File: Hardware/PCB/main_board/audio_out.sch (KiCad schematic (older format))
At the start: 28 parts, among them J12 Post_AB_amp, J13 Audio_out_jack, J6 AudioJack3, J9 Pre_AB_amp, Q1 BC857B, Q2 BC847B, Q3 BC847B, Q4 BC857B, U5 MCP6002-xSN

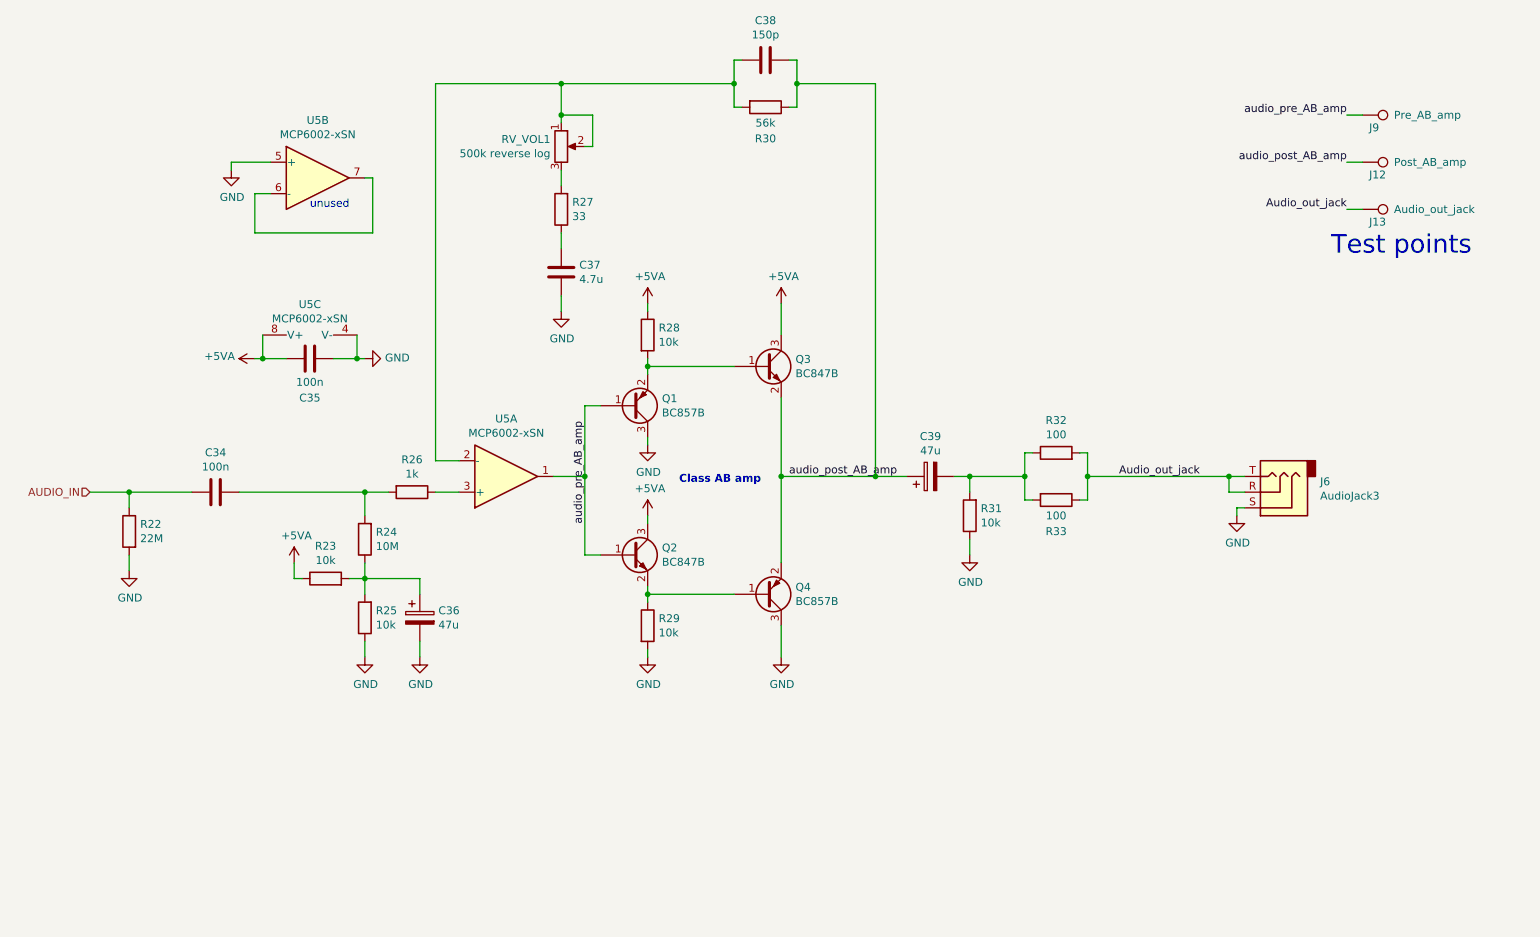
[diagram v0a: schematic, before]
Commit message: Use headphone amp IC instead of discrete amp
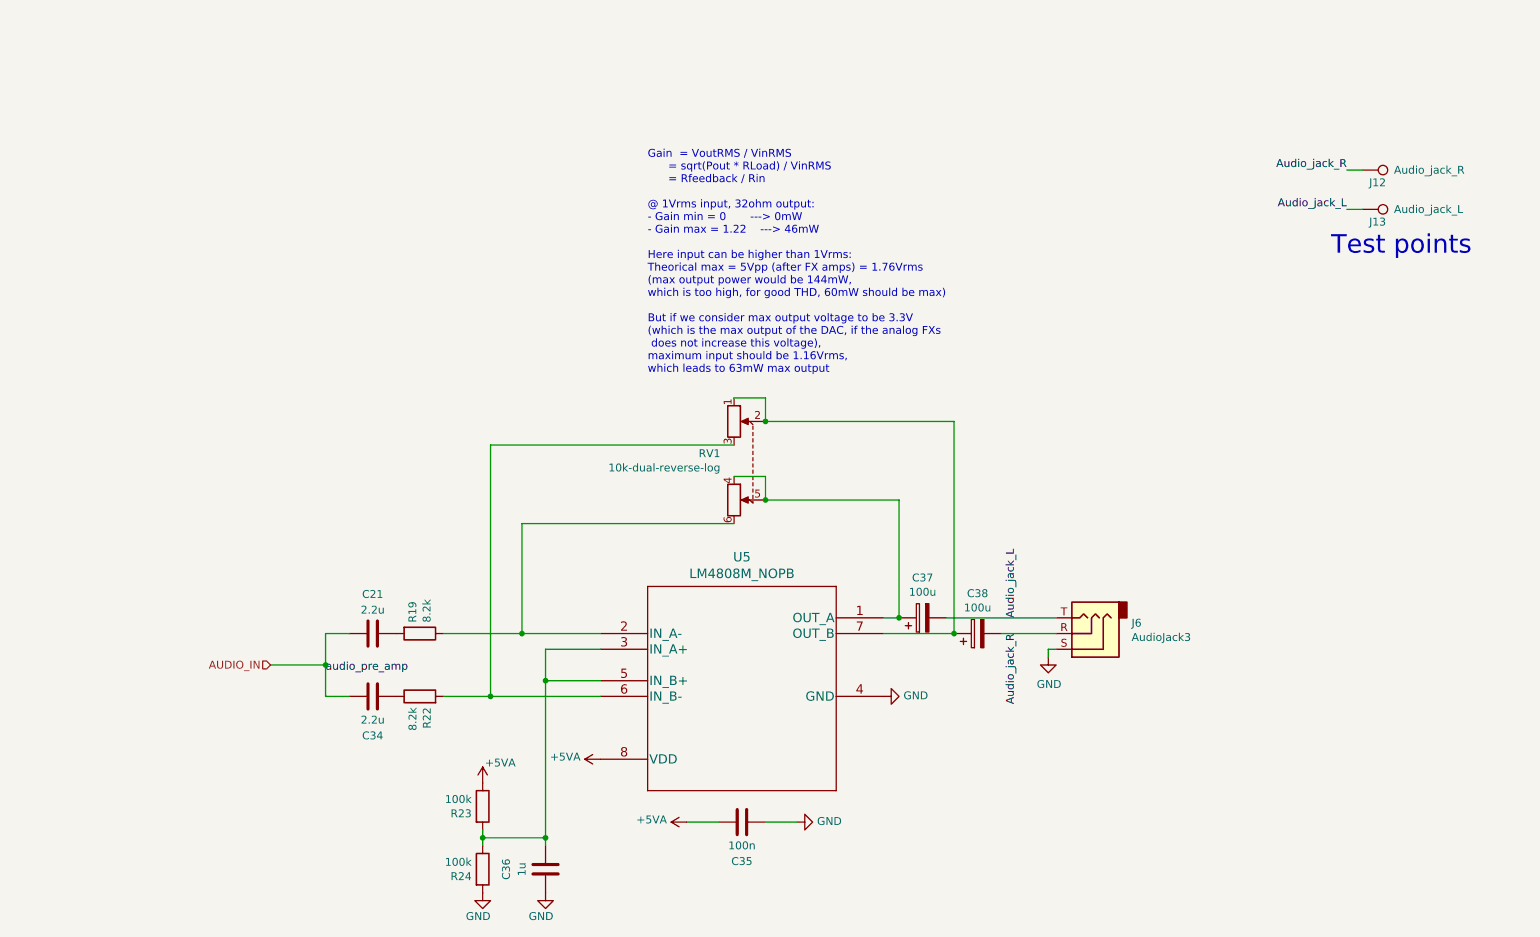
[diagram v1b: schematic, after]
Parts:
- removed C36, C39: 47u, Capacitor_SMD:CP_Elec_6.3x5.4, symbol Device:CP
- removed C37: 4.7u, Capacitor_SMD:C_0805_2012Metric, symbol Device:C
- removed C38: 150p, Capacitor_SMD:C_0805_2012Metric, symbol Device:C
- removed J9: Pre_AB_amp, TestPoint:TestPoint_THTPad_D1.0mm_Drill0.5mm, symbol Connector:TestPoint
- removed Q1, Q4: BC857B, Package_TO_SOT_SMD:SOT-23, symbol Transistor_BJT:BC857
- removed Q2, Q3: BC847B, Package_TO_SOT_SMD:SOT-23, symbol Transistor_BJT:BC847
- removed R25, R28, R29, R31: 10k, Resistor_SMD:R_0805_2012Metric, symbol Device:R
- removed R26: 1k, Resistor_SMD:R_0805_2012Metric, symbol Device:R
- removed R27: 33, Resistor_SMD:R_0805_2012Metric, symbol Device:R
- removed R30: 56k, Resistor_SMD:R_0805_2012Metric, symbol Device:R
- removed R32, R33: 100, Resistor_SMD:R_0805_2012Metric, symbol Device:R
- removed RV_VOL1: 500k reverse log, Potentiometer_THT:Potentiometer_Alps_RK09K_Single_Horizontal, symbol Device:R_POT
- removed U5: MCP6002-xSN, Package_SO:SOIC-8_3.9x4.9mm_P1.27mm, symbol Amplifier_Operational:MCP6002-xSN
- added C21: 2.2u, Capacitor_SMD:C_0805_2012Metric, symbol Device:C
- added C36: 1u, Capacitor_SMD:C_0805_2012Metric, symbol Device:C
- added C37, C38: 100u, Capacitor_SMD:CP_Elec_6.3x5.4, symbol Device:CP
- added R19: 8.2k, Resistor_SMD:R_0805_2012Metric, symbol Device:R
- added RV1: 10k-dual-reverse-log, Potentiometer_THT:Potentiometer_Alps_RK09L_Double_Horizontal, symbol Device:R_POT_Dual
- added U5: LM4808M_NOPB, lib:LM4808M&slash_NOPB, symbol LM4808:LM4808M_NOPB
- C34: value 100n -> 2.2u
- J12: value Post_AB_amp -> Audio_jack_R
- J13: value Audio_out_jack -> Audio_jack_L
- R22: value 22M -> 8.2k
- R23: value 10k -> 100k
- R24: value 10M -> 100k
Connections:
- net +5VA: now also U5.8 (VDD)
- net AUDIO_IN: now also C21.1; no longer R22.1
- net GND: now also R24.2, C36.1, U5.4 (GND); no longer R22.2
- net at C34.1: now also R22.1; no longer R24.2
- net at R23.2, R24.1: now also C36.2, U5.3 (IN_A+), U5.5 (IN_B+)
- net Audio_out_jack renamed Audio_jack_L
- net Audio_jack_L: now also C37.2; no longer J6.R
- net audio_post_AB_amp renamed Audio_jack_R
- net Audio_jack_R: now also J6.R, C38.2
- new net: C37.1, RV1.4, RV1.5, U5.1 (OUT_A)
- new net: R19.1, RV1.6, U5.2 (IN_A-)
- new net: R22.2, RV1.3, U5.6 (IN_B-)
- new net: C38.1, RV1.1, RV1.2, U5.7 (OUT_B)
- new net: C21.2, R19.2
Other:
- note added: "Gain = VoutRMS / VinRMS\n = sqrt(Pout * RLoad) / VinRMS\n = Rfeedback / Rin\n\n@ 1Vrms input, 32ohm output:\n- Gain min = 0 ---> 0mW\n- Gain max = 1.22 ---> 46mW\n\nHere input can be higher than 1Vrms:\nTheorical max = 5Vpp (after FX amps) = 1.76Vrms \n(max output power would be 144mW,\nwhich is too high, for good THD, 60mW should be max)\n\nBut if we consider max output voltage to be 3.3V \n(whi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"
- note removed: "Class AB amp"
- note removed: "unused"
- moved on the sheet: C35, J6
